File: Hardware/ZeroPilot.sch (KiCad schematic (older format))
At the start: 5 parts

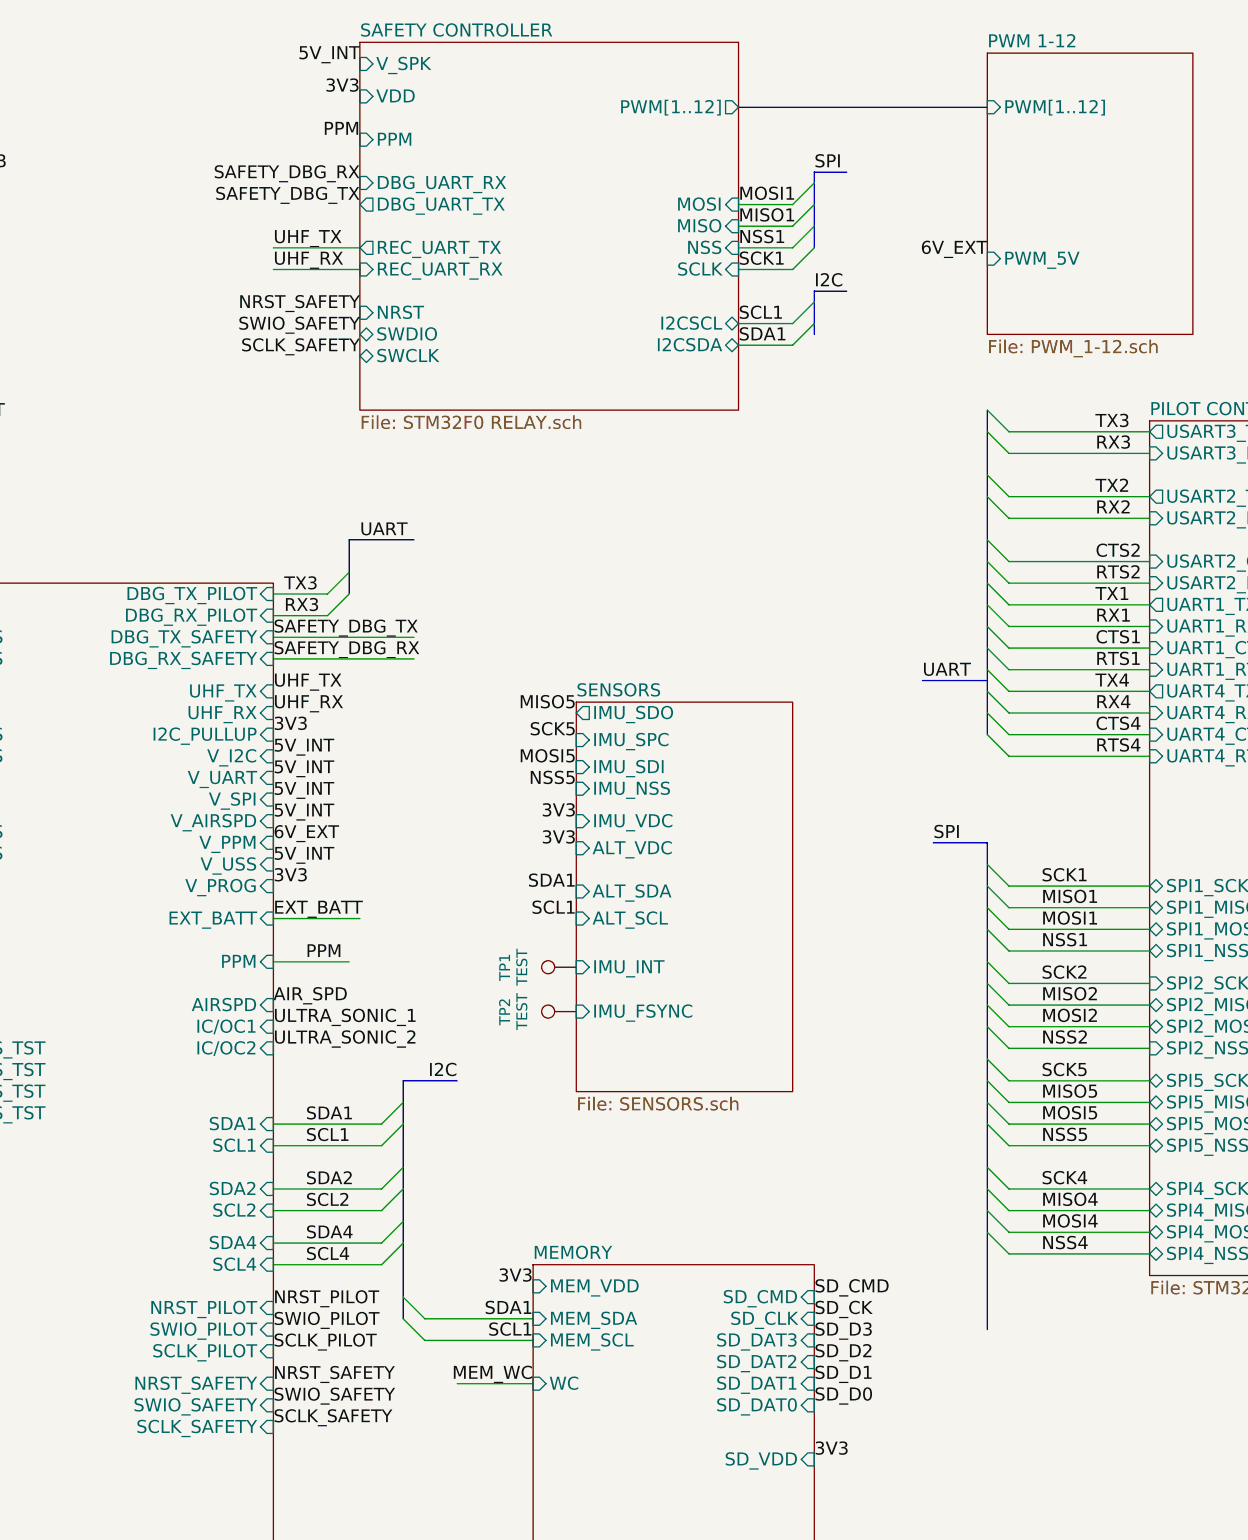
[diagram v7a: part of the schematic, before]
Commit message: Added RSSI, datasheets, INDU-004
Added RSSI input to PPM connector. Added datasheets for most of the components. The filter inductors for the FTDI were labeled as INDU-002, which is a 15uH smps inductor.
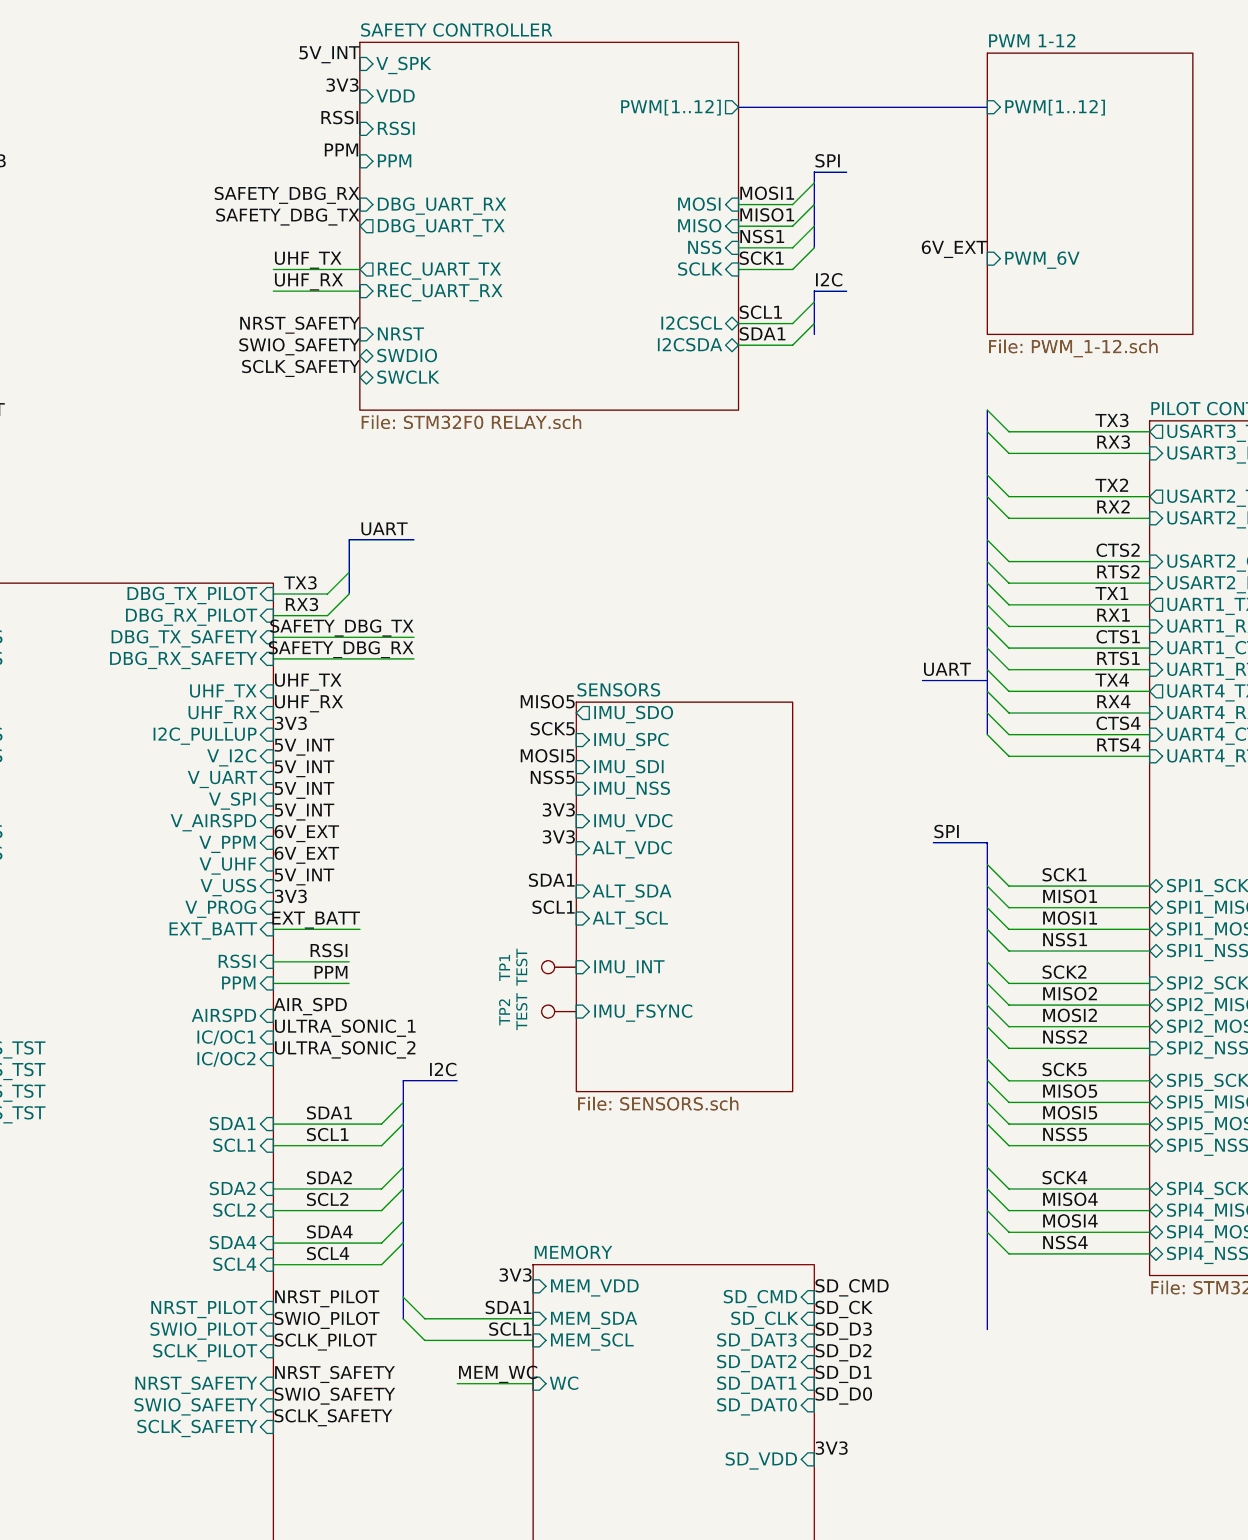
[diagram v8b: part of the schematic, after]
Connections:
- net labels added: RSSI
- wire segments 100 -> 101
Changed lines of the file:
@@
 F0 "PWM 1-12" 60
 F1 "PWM_1-12.sch" 60
-F2 "PWM_5V" I L 6450 1600 60
+F2 "PWM_6V" I L 6450 1600 60
 F3 "PWM[1..12]" I L 6450 900 60
 $EndSheet
@@
 F1 "STM32F0 RELAY.sch" 60
 F2 "VDD" I L 3550 850 60
-F3 "PPM" I L 3550 1050 60
+F3 "PPM" I L 3550 1150 60
 F4 "PWM[1..12]" O R 5300 900 60
 F5 "I2CSCL" B R 5300 1900 60
 F6 "I2CSDA" B R 5300 2000 60
-F7 "NRST" I L 3550 1850 60
-F8 "SWDIO" B L 3550 1950 60
-F9 "SWCLK" B L 3550 2050 60
-F10 "REC_UART_TX" O L 3550 1550 60
-F11 "REC_UART_RX" I L 3550 1650 60
-F12 "DBG_UART_RX" I L 3550 1250 60
-F13 "DBG_UART_TX" O L 3550 1350 60
+F7 "NRST" I L 3550 1950 60
+F8 "SWDIO" B L 3550 2050 60
+F9 "SWCLK" B L 3550 2150 60
+F10 "REC_UART_TX" O L 3550 1650 60
+F11 "REC_UART_RX" I L 3550 1750 60
+F12 "DBG_UART_RX" I L 3550 1350 60
+F13 "DBG_UART_TX" O L 3550 1450 60
 F14 "MOSI" I R 5300 1350 60
 F15 "MISO" I R 5300 1450 60
@@
 F17 "SCLK" I R 5300 1650 60
 F18 "V_SPK" I L 3550 700 60
+F19 "RSSI" I L 3550 1000 60
 $EndSheet
 $Sheet
@@
 Text Label 8950 5600 0    60   ~ 0
 MEM_WC
-Text Label 4350 6800 2    60   ~ 0
+Text Label 4000 6800 0    60   ~ 0
 MEM_WC
 Text Label 4350 6350 2    60   ~ 0
@@
 Text Label 6950 3900 0    60   ~ 0
 RTS4
-Text Label 3550 1050 2    60   ~ 0
+Text Label 3550 1150 2    60   ~ 0
 PPM
-Text Label 3150 1650 0    60   ~ 0
+Text Label 3150 1750 0    60   ~ 0
 UHF_RX
 Entry Wire Line
@@
 Text Label 3200 3250 0    59   ~ 0
 RX3
-Text Label 3550 1250 2    59   ~ 0
+Text Label 3550 1350 2    59   ~ 0
 SAFETY_DBG_RX
-Text Label 3150 3450 0    59   ~ 0
+Text Label 3800 3450 2    59   ~ 0
 SAFETY_DBG_RX
-Text Label 3550 1350 2    59   ~ 0
+Text Label 3550 1450 2    59   ~ 0
 SAFETY_DBG_TX
-Text Label 3150 3350 0    59   ~ 0
+Text Label 3800 3350 2    59   ~ 0
 SAFETY_DBG_TX
 Text Label 650  5700 0    60   ~ 0
@@
 Text Label 3300 6250 0    59   ~ 0
 SCL4
-Text Label 3300 4850 0    59   ~ 0
+Text Label 3500 4950 2    59   ~ 0
 PPM
-Text Label 3150 4650 0    60   ~ 0
+Text Label 3550 4700 2    60   ~ 0
 EXT_BATT
-Text Label 3150 5050 0    60   ~ 0
+Text Label 3150 5100 0    60   ~ 0
 AIR_SPD
-Text Label 3150 5150 0    60   ~ 0
+Text Label 3150 5200 0    60   ~ 0
 ULTRA_SONIC_1
-Text Label 3150 5250 0    60   ~ 0
+Text Label 3150 5300 0    60   ~ 0
 ULTRA_SONIC_2
 Text Label 3150 4100 0    59   ~ 0
@@
 Text Label 3150 4200 0    59   ~ 0
 5V_INT
-Text Label 3150 4400 0    59   ~ 0
+Text Label 3150 4500 0    59   ~ 0
 5V_INT
 Text Label 3150 4000 0    59   ~ 0
@@
 Text Label 3150 7000 0    59   ~ 0
 SCLK_SAFETY
-Text Label 3550 1850 2    59   ~ 0
+Text Label 3550 1950 2    59   ~ 0
 NRST_SAFETY
-Text Label 3550 1950 2    59   ~ 0
+Text Label 3550 2050 2    59   ~ 0
 SWIO_SAFETY
-Text Label 3550 2050 2    59   ~ 0
+Text Label 3550 2150 2    59   ~ 0
 SCLK_SAFETY
 $Comp
@@
 Text Label 5650 7150 0    60   ~ 0
 3V3
-Text Label 3150 4500 0    60   ~ 0
+Text Label 3150 4600 0    60   ~ 0
 3V3
 $Sheet
@@
 Text Label 10650 3550 0    60   ~ 0
 EXT_BATT
-Text Label 3150 1550 0    60   ~ 0
+Text Label 3150 1650 0    60   ~ 0
 UHF_TX
 Text Label 3150 3600 0    60   ~ 0
@@
 	6550 2800 7200 2800
 Wire Wire Line
-	3150 1650 3550 1650
+	3150 1750 3550 1750
 Wire Wire Line
 	6550 2400 7200 2400
@@
 	3650 5600 3150 5600
 Wire Wire Line
-	3150 4850 3500 4850
-Wire Wire Line
-	3150 4650 3550 4650
+	3150 4950 3500 4950
+Wire Wire Line
+	3150 4700 3550 4700
 Wire Wire Line
 	8950 2800 10500 2800
@@
 	9900 3850 8950 3850
 Wire Wire Line
-	3550 1550 3150 1550
+	3550 1650 3150 1650
 Wire Bus Line
 	5800 1200 5650 1200
@@
 F0 "HEADERS" 60
 F1 "HEADERS.sch" 60
-F2 "EXT_BATT" I R 3150 4650 60
+F2 "EXT_BATT" I R 3150 4700 60
 F3 "DBG_RX_SAFETY" I R 3150 3450 60
 F4 "DBG_TX_SAFETY" I R 3150 3350 60
@@
 F31 "SPI5_SI" I L 1350 7400 60
 F32 "SPI5_CK" I L 1350 7200 60
-F33 "IC/OC1" I R 3150 5150 60
-F34 "IC/OC2" I R 3150 5250 60
-F35 "V_USS" I R 3150 4400 60
+F33 "IC/OC1" I R 3150 5200 60
+F34 "IC/OC2" I R 3150 5300 60
+F35 "V_USS" I R 3150 4500 60
 F36 "V_AIRSPD" I R 3150 4200 60
-F37 "AIRSPD" I R 3150 5050 60
+F37 "AIRSPD" I R 3150 5100 60
 F38 "V_PPM" I R 3150 4300 60
-F39 "PPM" I R 3150 4850 60
+F39 "PPM" I R 3150 4950 60
 F40 "SPI1_SS" I L 1350 6150 60
 F41 "SPI1_SDO" I L 1350 5950 60
@@
 F55 "SWIO_SAFETY" I R 3150 6900 60
 F56 "SCLK_SAFETY" I R 3150 7000 60
-F57 "V_PROG" I R 3150 4500 60
+F57 "V_PROG" I R 3150 4600 60
 F58 "UHF_RX" I R 3150 3700 60
 F59 "UHF_TX" I R 3150 3600 60
@@
 F67 "UART2_RTS_TST" I L 1350 5450 60
 F68 "UART2_CTS_TST" I L 1350 5550 60
+F69 "RSSI" I R 3150 4850 60
+F70 "V_UHF" I R 3150 4400 60
 $EndSheet
 Text Label 1350 5250 2    60   ~ 0
@@
 Text Label 5650 6400 0    60   ~ 0
 SD_CMD
+Wire Wire Line
+	3150 4850 3500 4850
+Text Label 3500 4850 2    60   ~ 0
+RSSI
+Text Label 3550 1000 2    60   ~ 0
+RSSI
+Text Label 3150 4400 0    59   ~ 0
+6V_EXT
 Wire Bus Line
 	9750 4200 9750 4500
